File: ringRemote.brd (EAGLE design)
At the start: 100 x 80 mm, 13 parts, among them Y1 32.768kHz

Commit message: added a todo list; did some thinking for the HMI pushbuttons
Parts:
- added R1, R4, R5, R6: 100k, ringRemote:0201
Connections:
- new net 3.3V: R1.2, R4.2, R5.2, R6.2
- new net N$6: R4.1, U$1.P$12
- new net N$7: R1.1, U$1.P$11
- new net N$8: R5.1, U$1.P$19
- new net N$9: R6.1, U$1.P$20
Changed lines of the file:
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@@
 <element name="C6" library="ringRemote" package="0201" value="1uF" x="-109.22" y="-33.02"/>
 <element name="R3" library="ringRemote" package="0201" value="100k" x="-109.22" y="-36.83"/>
+<element name="R1" library="ringRemote" package="0201" value="100k" x="-109.22" y="-40.64"/>
+<element name="R4" library="ringRemote" package="0201" value="100k" x="-109.22" y="-44.45"/>
+<element name="R5" library="ringRemote" package="0201" value="100k" x="-109.22" y="-48.26"/>
+<element name="R6" library="ringRemote" package="0201" value="100k" x="-109.22" y="-52.07"/>
 </elements>
 <signals>
@@
 <wire x1="-1.375" y1="-22.51" x2="-103.2185" y2="-20.6155" width="0" layer="19" extent="1-1"/>
 </signal>
+<signal name="N$6">
+<contactref element="R4" pad="1"/>
+<contactref element="U$1" pad="P$12"/>
+<wire x1="-1.375" y1="-18.51" x2="-109.22" y2="-44.175" width="0" layer="19" extent="1-1"/>
+</signal>
+<signal name="N$7">
+<contactref element="U$1" pad="P$11"/>
+<contactref element="R1" pad="1"/>
+<wire x1="-0.75" y1="-18.51" x2="-109.22" y2="-40.365" width="0" layer="19" extent="1-1"/>
+</signal>
+<signal name="N$8">
+<contactref element="U$1" pad="P$19"/>
+<contactref element="R5" pad="1"/>
+<wire x1="-4" y1="-21.135" x2="-109.22" y2="-47.985" width="0" layer="19" extent="1-1"/>
+</signal>
+<signal name="N$9">
+<contactref element="U$1" pad="P$20"/>
+<contactref element="R6" pad="1"/>
+<wire x1="-4" y1="-21.76" x2="-109.22" y2="-51.795" width="0" layer="19" extent="1-1"/>
+</signal>
+<signal name="3.3V">
+<contactref element="R6" pad="2"/>
+<contactref element="R5" pad="2"/>
+<contactref element="R1" pad="2"/>
+<contactref element="R4" pad="2"/>
+<wire x1="-109.22" y1="-48.535" x2="-109.22" y2="-52.345" width="0" layer="19" extent="1-1"/>
+<wire x1="-109.22" y1="-44.725" x2="-109.22" y2="-48.535" width="0" layer="19" extent="1-1"/>
+<wire x1="-109.22" y1="-40.915" x2="-109.22" y2="-44.725" width="0" layer="19" extent="1-1"/>
+</signal>
 </signals>

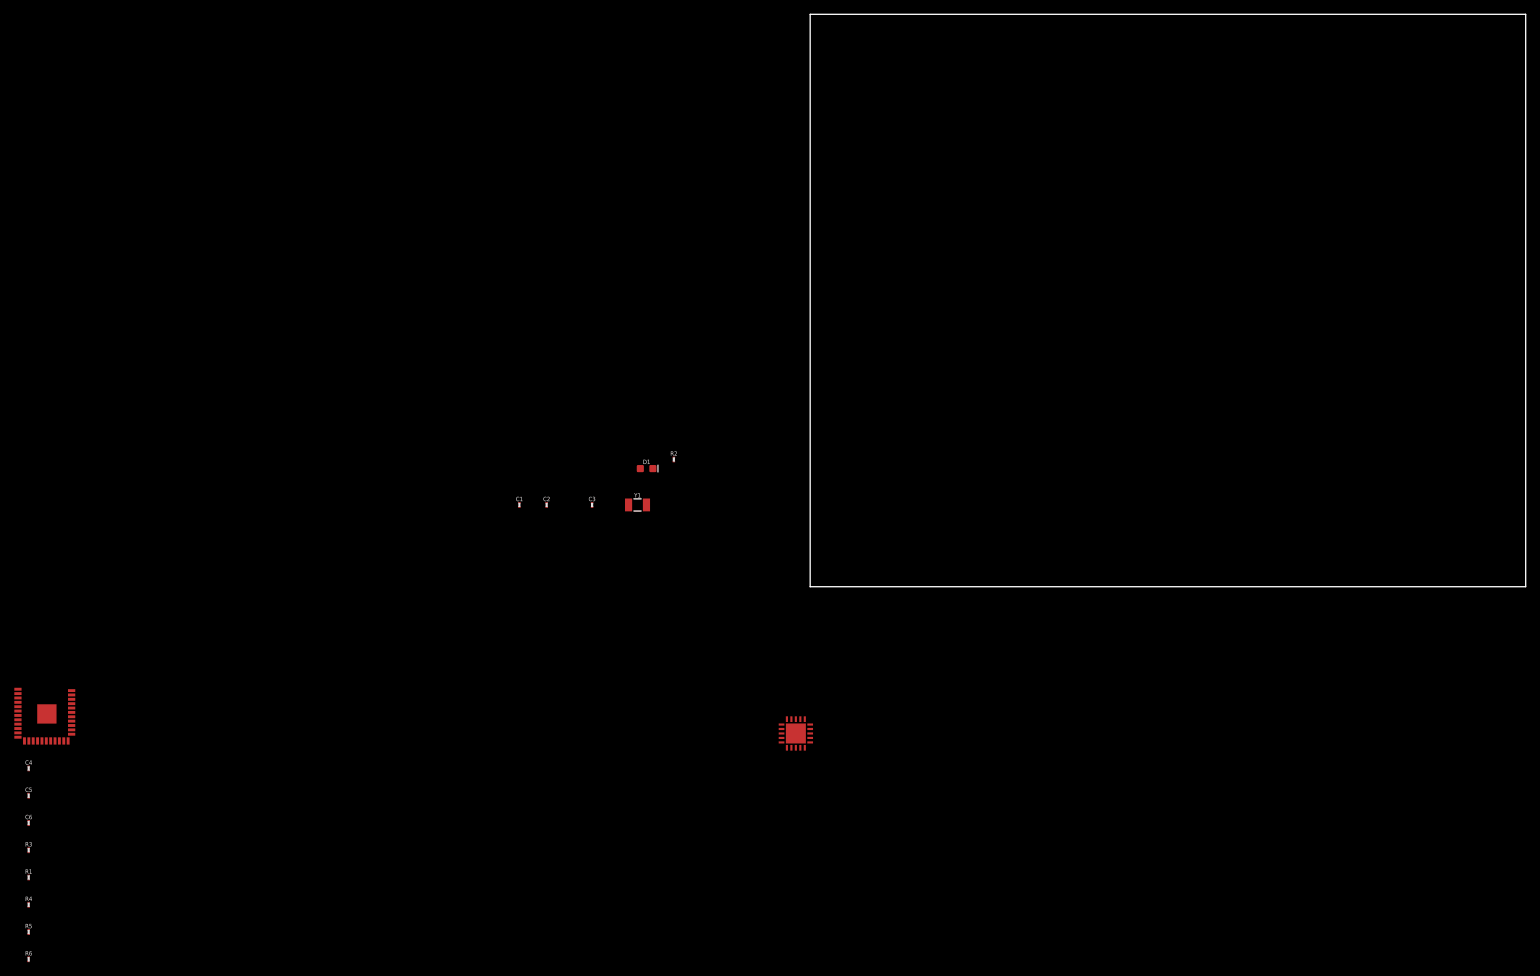
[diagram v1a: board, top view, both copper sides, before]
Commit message: added to bom: battery supervisor, charging circuit components; put components on board space to estimate stuff
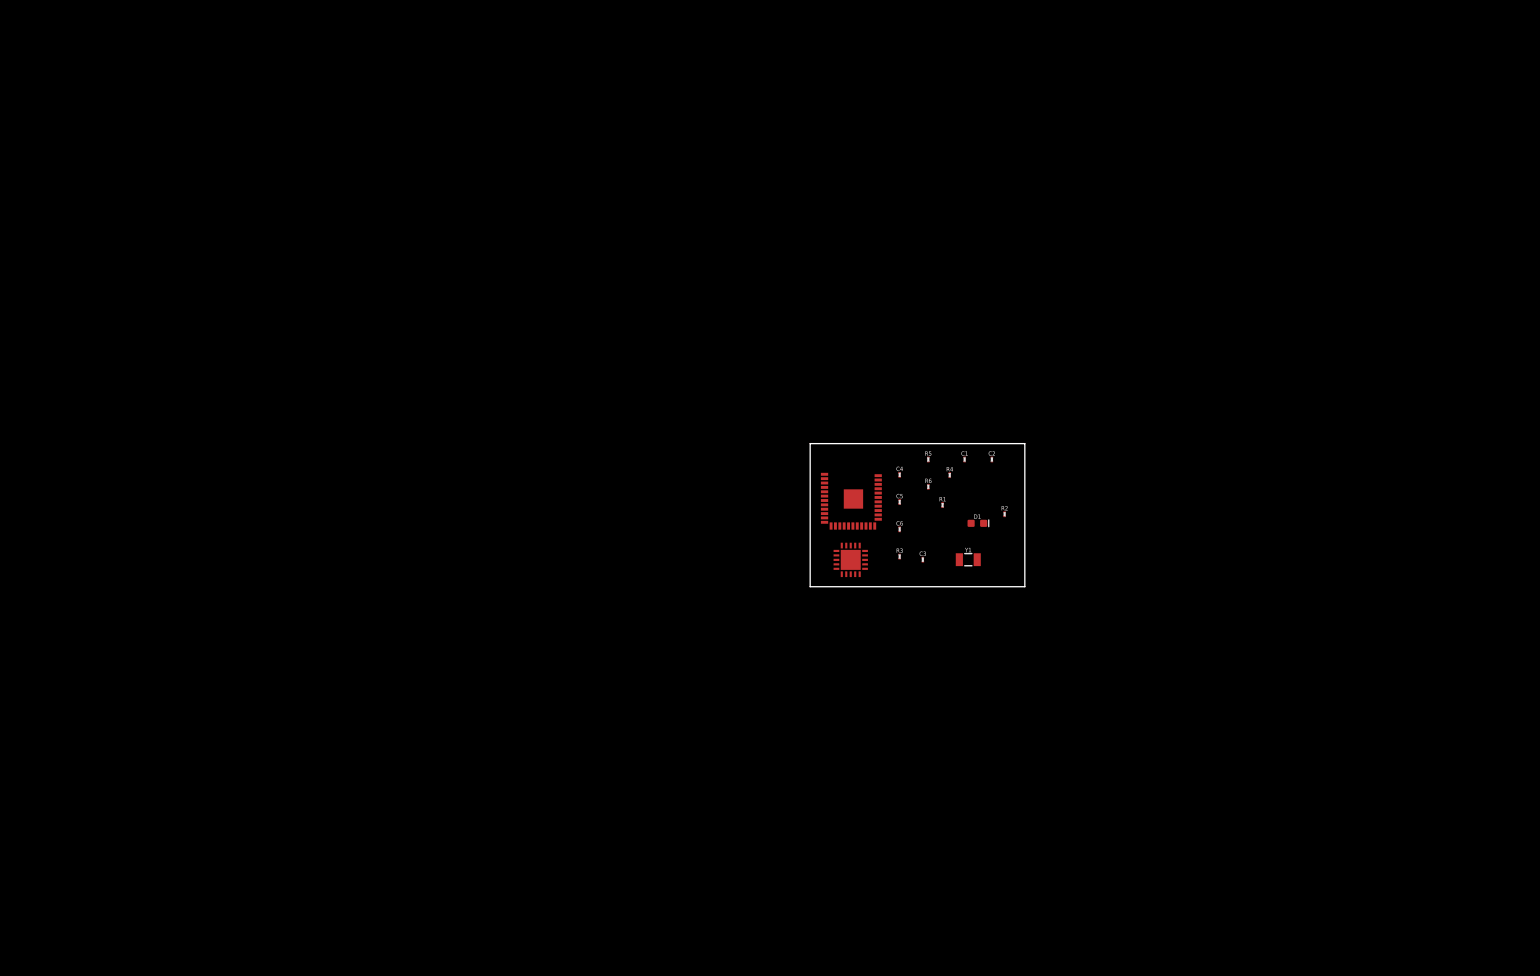
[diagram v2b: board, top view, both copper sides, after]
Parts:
- removed FRAME1: FRAME-LETTER, SparkFun-Aesthetics:CREATIVE_COMMONS
- moved R4 142.0 mm to (19.5, 15.6)
- moved R5 142.0 mm to (16.5, 17.8)
- moved R6 142.0 mm to (16.5, 14.0)
- moved R1 137.9 mm to (18.5, 11.4)
- moved C4 128.5 mm to (12.5, 15.6)
- moved C5 128.5 mm to (12.5, 11.8)
- moved C6 128.5 mm to (12.5, 8.02)
- moved R3 128.5 mm to (12.5, 4.21)
- moved U$2 116.7 mm to (6.05, 12.3)
- moved C1 62.6 mm to (21.6, 17.8)
- moved C2 62.6 mm to (25.4, 17.8)
- moved C3 46.9 mm to (15.8, 3.78)
- moved D1 46.9 mm to (23.4, 8.86)
- moved R2 46.9 mm to (27.2, 10.1)
- moved Y1 46.9 mm to (22.1, 3.78)
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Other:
- board size 100 x 80 mm -> 30 x 20 mm

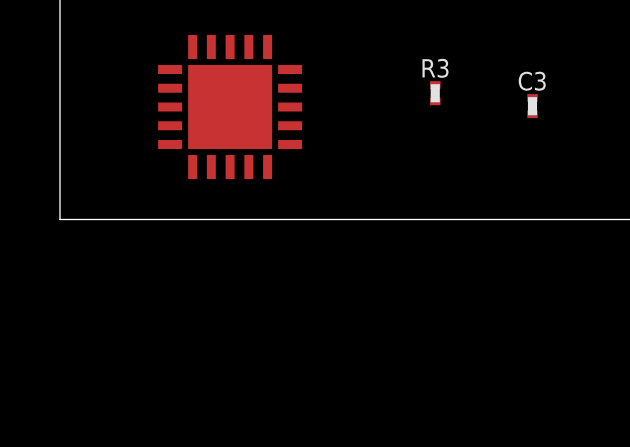
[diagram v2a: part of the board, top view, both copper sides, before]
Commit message: added battery supervisor part, wired it up
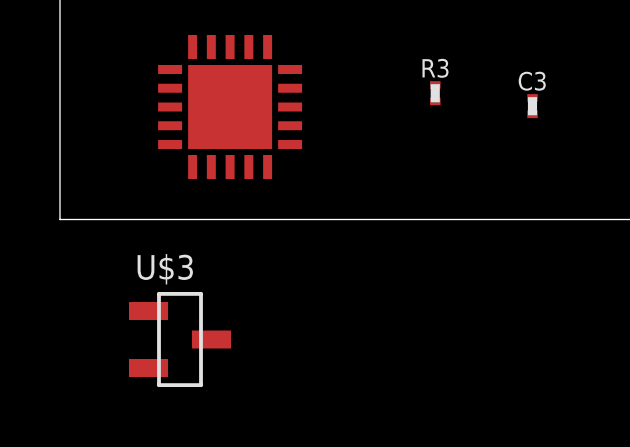
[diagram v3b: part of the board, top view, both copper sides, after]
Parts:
- added FRAME1: FRAME-LETTERNO_PACKAGE, SparkFun-Aesthetics:DUMMY
- added U$3: TPS3839, ringRemote:3-SOT-23
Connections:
- removed net 3.3V: R1.2, R4.2, R5.2, R6.2
- new net MAXRST: U$1.P$5, U$3.P$2
- net GND: now also R1.2, R4.2, R5.2, R6.2, U$3.P$1
- net VBAT: now also U$3.P$3
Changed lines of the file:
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@@
 <element name="R5" library="ringRemote" package="0201" value="100k" x="16.51" y="17.78"/>
 <element name="R6" library="ringRemote" package="0201" value="100k" x="16.51" y="13.97"/>
+<element name="U$3" library="ringRemote" package="3-SOT-23" value="TPS3839" x="4" y="-4"/>
+<element name="FRAME1" library="SparkFun-Aesthetics" package="DUMMY" value="FRAME-LETTERNO_PACKAGE" x="0" y="-6">
+<attribute name="DESIGNER" value="Nobody" x="0" y="-6" size="1.778" layer="27" display="off"/>
+<attribute name="VERSION" value="v01" x="0" y="-6" size="1.778" layer="27" display="off"/>
+</element>
 </elements>
 <signals>
@@
 <contactref element="U$2" pad="P$26"/>
 <contactref element="D1" pad="C"/>
-<wire x1="12.51" y1="11.555" x2="12.51" y2="7.745" width="0" layer="19" extent="1-1"/>
-<wire x1="12.51" y1="15.365" x2="12.51" y2="11.555" width="0" layer="19" extent="1-1"/>
-<wire x1="4.1425" y1="8.4845" x2="12.51" y2="15.365" width="0" layer="19" extent="1-1"/>
-<wire x1="6.05" y1="12.26" x2="4.1425" y2="8.4845" width="0" layer="19" extent="1-1"/>
-<wire x1="9.5115" y1="15.5245" x2="6.05" y2="12.26" width="0" layer="19" extent="1-1"/>
-<wire x1="21.59" y1="17.505" x2="9.5115" y2="15.5245" width="0" layer="19" extent="1-1"/>
-<wire x1="25.4" y1="17.505" x2="21.59" y2="17.505" width="0" layer="19" extent="1-1"/>
-<wire x1="15.75" y1="3.505" x2="25.4" y2="17.505" width="0" layer="19" extent="1-1"/>
-<wire x1="24.247" y1="8.86" x2="15.75" y2="3.505" width="0" layer="19" extent="1-1"/>
-<wire x1="5.67" y1="3.75" x2="24.247" y2="8.86" width="0" layer="19" extent="1-1"/>
+<contactref element="R6" pad="2"/>
+<contactref element="R5" pad="2"/>
+<contactref element="R1" pad="2"/>
+<contactref element="R4" pad="2"/>
+<contactref element="U$3" pad="P$1"/>
+<wire x1="21.59" y1="17.505" x2="25.4" y2="17.505" width="0" layer="19" extent="1-1"/>
+<wire x1="19.51" y1="15.315" x2="21.59" y2="17.505" width="0" layer="19" extent="1-1"/>
+<wire x1="16.51" y1="13.695" x2="19.51" y2="15.315" width="0" layer="19" extent="1-1"/>
+<wire x1="18.51" y1="11.125" x2="16.51" y2="13.695" width="0" layer="19" extent="1-1"/>
+<wire x1="16.51" y1="17.505" x2="19.51" y2="15.315" width="0" layer="19" extent="1-1"/>
+<wire x1="12.51" y1="15.365" x2="16.51" y2="13.695" width="0" layer="19" extent="1-1"/>
+<wire x1="9.5115" y1="15.5245" x2="12.51" y2="15.365" width="0" layer="19" extent="1-1"/>
+<wire x1="12.51" y1="11.555" x2="12.51" y2="15.365" width="0" layer="19" extent="1-1"/>
+<wire x1="12.51" y1="7.745" x2="12.51" y2="11.555" width="0" layer="19" extent="1-1"/>
+<wire x1="6.05" y1="12.26" x2="9.5115" y2="15.5245" width="0" layer="19" extent="1-1"/>
+<wire x1="4.1425" y1="8.4845" x2="6.05" y2="12.26" width="0" layer="19" extent="1-1"/>
+<wire x1="5.67" y1="3.75" x2="4.1425" y2="8.4845" width="0" layer="19" extent="1-1"/>
 <wire x1="7.67" y1="2.5" x2="5.67" y2="3.75" width="0" layer="19" extent="1-1"/>
+<wire x1="15.75" y1="3.505" x2="12.51" y2="7.745" width="0" layer="19" extent="1-1"/>
+<wire x1="24.247" y1="8.86" x2="18.51" y2="11.125" width="0" layer="19" extent="1-1"/>
+<wire x1="2.95" y1="-3.05" x2="7.67" y2="2.5" width="0" layer="19" extent="1-1"/>
 </signal>
 <signal name="VBAT">
@@
 <contactref element="C3" pad="1"/>
 <contactref element="U$1" pad="P$9"/>
-<wire x1="21.59" y1="18.055" x2="4.7525" y2="8.4845" width="0" layer="19" extent="1-1"/>
+<contactref element="U$3" pad="P$3"/>
 <wire x1="15.75" y1="4.055" x2="21.59" y2="18.055" width="0" layer="19" extent="1-1"/>
 <wire x1="7.67" y1="4.375" x2="15.75" y2="4.055" width="0" layer="19" extent="1-1"/>
+<wire x1="4.7525" y1="8.4845" x2="7.67" y2="4.375" width="0" layer="19" extent="1-1"/>
+<wire x1="5.05" y1="-4" x2="7.67" y2="4.375" width="0" layer="19" extent="1-1"/>
 </signal>
 <signal name="N$4">
@@
 <wire x1="3.67" y1="2.5" x2="16.51" y2="14.245" width="0" layer="19" extent="1-1"/>
 </signal>
-<signal name="3.3V">
-<contactref element="R6" pad="2"/>
-<contactref element="R5" pad="2"/>
-<contactref element="R1" pad="2"/>
-<contactref element="R4" pad="2"/>
-<wire x1="16.51" y1="17.505" x2="16.51" y2="13.695" width="0" layer="19" extent="1-1"/>
-<wire x1="19.51" y1="15.315" x2="16.51" y2="17.505" width="0" layer="19" extent="1-1"/>
-<wire x1="18.51" y1="11.125" x2="19.51" y2="15.315" width="0" layer="19" extent="1-1"/>
+<signal name="MAXRST">
+<contactref element="U$1" pad="P$5"/>
+<contactref element="U$3" pad="P$2"/>
+<wire x1="2.95" y1="-4.95" x2="6.92" y2="1.75" width="0" layer="19" extent="1-1"/>
 </signal>
 </signals>

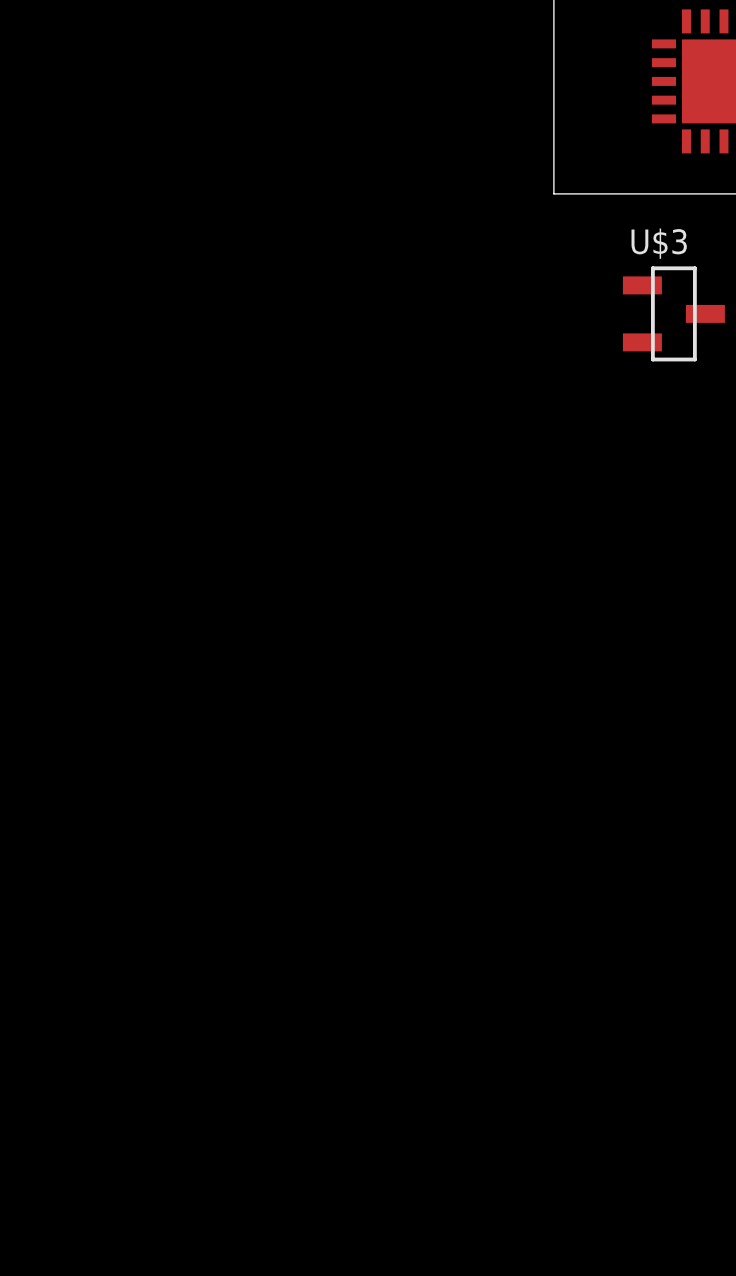
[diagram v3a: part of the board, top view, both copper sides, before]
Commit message: made a new sheet, moved all power stuff to second sheet; added charger circuit; added connector; added battery. pretty much just need to determine the programming interface before I start doing board layout
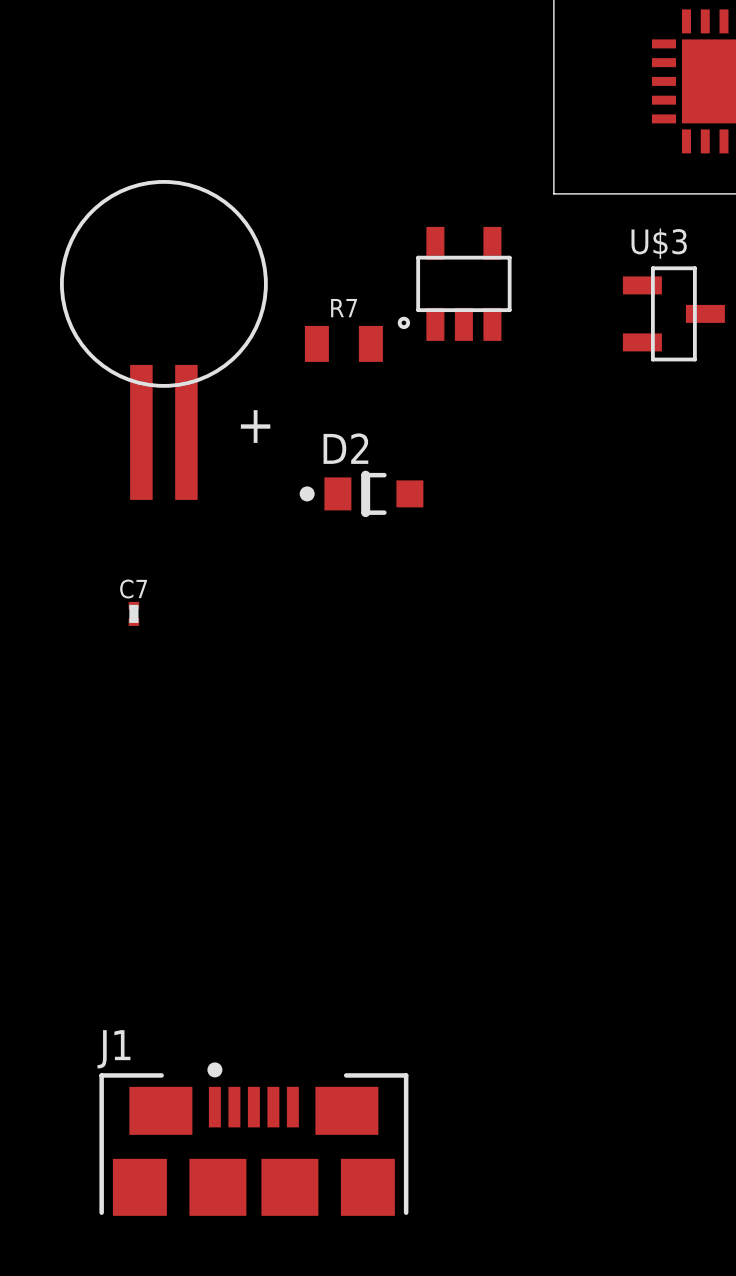
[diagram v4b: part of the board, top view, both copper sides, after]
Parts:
- added C7: 1uF, ringRemote:0201
- added D2: PANASONIC_DB2J31400LPANASONIC_DB2J31400L_0_0, ringRemote:PANASONIC_DB2J31400L_0
- added FRAME2: FRAME-LETTERNO_PACKAGE, SparkFun-Aesthetics:DUMMY
- added J1: AMPHENOL_10118192-0001LFAMPHENOL_10118192-0001LF_0_0, ringRemote:AMPHENOL_10118192-0001LF_0
- added R7: 1.8k, ringRemote:0805
- added U$4: TLV700, ringRemote:SOT-23-THIN
- added U$5: ML621S, ringRemote:ML621S
- U$3: value TPS3839 -> TPS3839G25
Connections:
- new net D+: J1.3
- new net D-: J1.2
- new net N$10: D2.2, U$4.P$5
- new net VCC: C1.1, C3.1, D2.1, R7.2, U$1.P$9, U$2.P$27, U$3.P$3
- new net VUSB: C7.1, J1.1, U$4.P$1, U$4.P$3
- net GND: now also C7.2, J1.10, J1.11, J1.5, J1.6, J1.7, J1.8, J1.9, U$4.P$2, U$5.P$2
- net VBAT: now also R7.1, U$5.P$1; no longer C1.1, C3.1, U$1.P$9, U$2.P$27, U$3.P$3
